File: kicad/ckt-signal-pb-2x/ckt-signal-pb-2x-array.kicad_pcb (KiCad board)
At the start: 2 copper layers, 81.9 x 157.4 mm, 144 parts, among them J1 Molex 0532610471, J2 Molex 0532610471

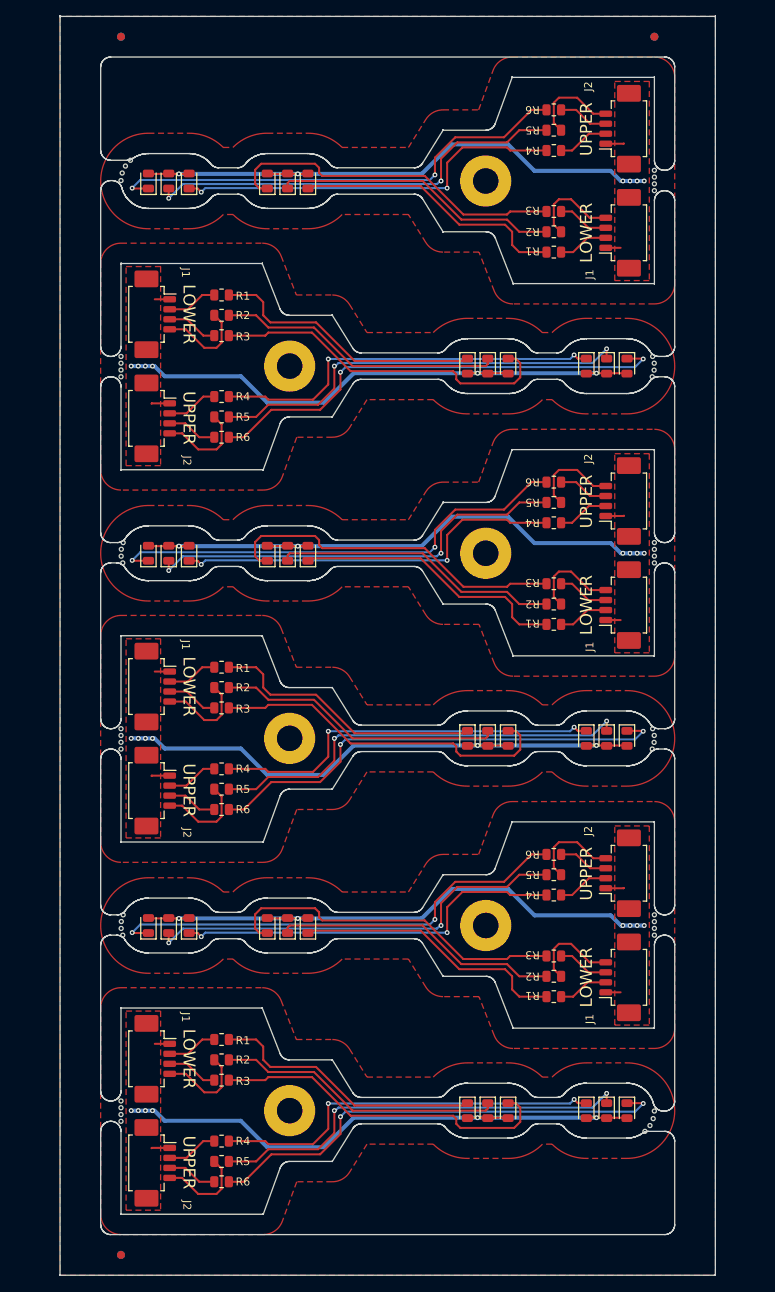
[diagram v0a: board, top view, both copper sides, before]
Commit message: Redesign 2x signal for better panelization
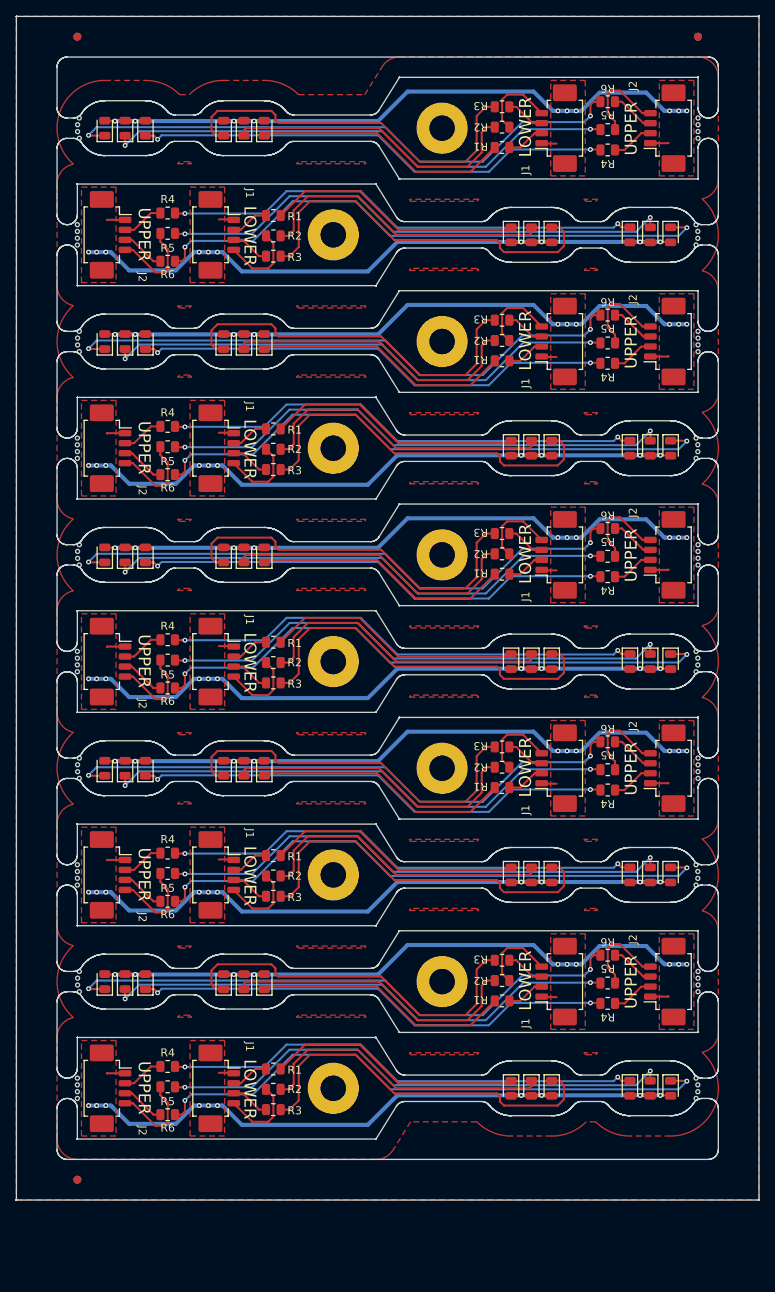
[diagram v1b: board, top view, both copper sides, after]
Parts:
- removed the D1 at (138.5, 133.6)
- removed the D1 at (138.5, 87.1)
- removed the D1 at (158.5, 156.8)
- removed the D1 at (158.5, 110.2)
- removed the D1 at (158.5, 63.7)
- removed the D1 at (138.5, 40.6)
- removed the D2 at (161.0, 156.8)
- removed the D2 at (136.0, 133.6)
- removed the D2 at (136.0, 87.1)
- removed the D2 at (161.0, 63.7)
- removed the D2 at (161.0, 110.2)
- removed the D2 at (136.0, 40.6)
- removed the D3 at (163.5, 63.7)
- removed the D3 at (133.5, 87.1)
- removed the D3 at (163.5, 110.2)
- removed the D3 at (133.5, 40.6)
- removed the D3 at (133.5, 133.6)
- removed the D3 at (163.5, 156.8)
- removed the D4 at (173.3, 156.8)
- removed the D4 at (173.3, 63.7)
- removed the D4 at (123.7, 40.6)
- removed the D4 at (123.7, 87.1)
- removed the D4 at (173.3, 110.2)
- removed the D4 at (123.7, 133.6)
- removed the D5 at (175.9, 110.2)
- removed the D5 at (121.1, 133.6)
- removed the D5 at (175.9, 156.8)
- removed the D5 at (121.1, 87.1)
- removed the D5 at (175.9, 63.7)
- removed the D5 at (121.1, 40.6)
- removed the D6 at (178.4, 156.8)
- removed the D6 at (118.6, 133.6)
- removed the D6 at (118.6, 87.1)
- removed the D6 at (178.4, 63.7)
- removed the D6 at (118.6, 40.6)
- removed the D6 at (178.4, 110.2)
- removed the H1 at (136.2, 156.8)
- removed the H1 at (136.2, 63.7)
- removed the H1 at (160.8, 40.6)
- removed the H1 at (160.8, 133.6)
- removed the H1 at (160.8, 87.1)
- removed the H1 at (136.2, 110.2)
- removed the J1 at (178.2, 93.6)
- removed the J1 at (178.2, 140.1)
- removed the J1 at (118.8, 150.3)
- removed the J1 at (118.8, 103.8)
- removed the J1 at (178.2, 47.1)
- removed the J1 at (118.8, 57.2)
- removed the J2 at (178.2, 127.1)
- removed the J2 at (118.8, 116.8)
- removed the J2 at (118.8, 163.3)
- removed the J2 at (118.8, 70.2)
- removed the J2 at (178.2, 80.6)
- removed the J2 at (178.2, 34.0)
- removed the R1 at (169.3, 49.5)
- removed the R1 at (169.3, 142.5)
- removed the R1 at (127.7, 147.9)
- removed the R1 at (127.7, 101.4)
- removed the R1 at (169.3, 96.0)
- removed the R1 at (127.7, 54.8)
- removed the R2 at (169.3, 93.5)
- removed the R2 at (127.7, 150.4)
- removed the R2 at (169.3, 140.0)
- removed the R2 at (127.7, 103.9)
- removed the R2 at (127.7, 57.4)
- removed the R2 at (169.3, 46.9)
- removed the R3 at (127.7, 59.9)
- removed the R3 at (169.3, 137.4)
- removed the R3 at (127.7, 153.0)
- removed the R3 at (169.3, 90.9)
- removed the R3 at (169.3, 44.4)
- removed the R3 at (127.7, 106.4)
- removed the R4 at (169.3, 129.8)
- removed the R4 at (127.7, 67.5)
- removed the R4 at (127.7, 114.1)
- removed the R4 at (127.7, 160.6)
- removed the R4 at (169.3, 83.3)
- removed the R4 at (169.3, 36.8)
- removed the R5 at (127.7, 116.6)
- removed the R5 at (169.3, 127.3)
- removed the R5 at (127.7, 70.1)
- removed the R5 at (169.3, 80.8)
- removed the R5 at (169.3, 34.2)
- removed the R5 at (127.7, 163.1)
- removed the R6 at (127.7, 165.7)
- removed the R6 at (169.3, 124.7)
- removed the R6 at (127.7, 72.6)
- removed the R6 at (169.3, 78.2)
- removed the R6 at (169.3, 31.7)
- removed the R6 at (127.7, 119.1)
- added D1: RED, LED_SMD:LED_0805_2012Metric, F.Cu at (133.1, 60.6)
- added D1: RED, LED_SMD:LED_0805_2012Metric, F.Cu at (163.9, 127.3)
- added D1: RED, LED_SMD:LED_0805_2012Metric, F.Cu at (133.1, 87.3)
- added D1: RED, LED_SMD:LED_0805_2012Metric, F.Cu at (133.1, 140.7)
- added D1: RED, LED_SMD:LED_0805_2012Metric, F.Cu at (163.9, 47.3)
- added D1: RED, LED_SMD:LED_0805_2012Metric, F.Cu at (133.1, 34.0)
- added D1: RED, LED_SMD:LED_0805_2012Metric, F.Cu at (133.1, 114.0)
- added D1: RED, LED_SMD:LED_0805_2012Metric, F.Cu at (163.9, 74.0)
- added D1: RED, LED_SMD:LED_0805_2012Metric, F.Cu at (163.9, 154.0)
- added D1: RED, LED_SMD:LED_0805_2012Metric, F.Cu at (163.9, 100.6)
- added D2: AMBER, LED_SMD:LED_0805_2012Metric, F.Cu at (130.5, 114.0)
- added D2: AMBER, LED_SMD:LED_0805_2012Metric, F.Cu at (166.5, 74.0)
- added D2: AMBER, LED_SMD:LED_0805_2012Metric, F.Cu at (130.5, 60.6)
- added D2: AMBER, LED_SMD:LED_0805_2012Metric, F.Cu at (130.5, 87.3)
- added D2: AMBER, LED_SMD:LED_0805_2012Metric, F.Cu at (130.5, 34.0)
- added D2: AMBER, LED_SMD:LED_0805_2012Metric, F.Cu at (130.5, 140.7)
- added D2: AMBER, LED_SMD:LED_0805_2012Metric, F.Cu at (166.5, 127.3)
- added D2: AMBER, LED_SMD:LED_0805_2012Metric, F.Cu at (166.5, 47.3)
- added D2: AMBER, LED_SMD:LED_0805_2012Metric, F.Cu at (166.5, 154.0)
- added D2: AMBER, LED_SMD:LED_0805_2012Metric, F.Cu at (166.5, 100.6)
- added D3: GREEN, LED_SMD:LED_0805_2012Metric, F.Cu at (128.0, 87.3)
- added D3: GREEN, LED_SMD:LED_0805_2012Metric, F.Cu at (169.0, 100.6)
- added D3: GREEN, LED_SMD:LED_0805_2012Metric, F.Cu at (169.0, 74.0)
- added D3: GREEN, LED_SMD:LED_0805_2012Metric, F.Cu at (128.0, 114.0)
- added D3: GREEN, LED_SMD:LED_0805_2012Metric, F.Cu at (128.0, 34.0)
- added D3: GREEN, LED_SMD:LED_0805_2012Metric, F.Cu at (128.0, 60.6)
- added D3: GREEN, LED_SMD:LED_0805_2012Metric, F.Cu at (128.0, 140.7)
- added D3: GREEN, LED_SMD:LED_0805_2012Metric, F.Cu at (169.0, 47.3)
- added D3: GREEN, LED_SMD:LED_0805_2012Metric, F.Cu at (169.0, 127.3)
- added D3: GREEN, LED_SMD:LED_0805_2012Metric, F.Cu at (169.0, 154.0)
- added D4: RED, LED_SMD:LED_0805_2012Metric, F.Cu at (118.2, 87.3)
- added D4: RED, LED_SMD:LED_0805_2012Metric, F.Cu at (118.2, 140.7)
- added D4: RED, LED_SMD:LED_0805_2012Metric, F.Cu at (178.8, 47.3)
- added D4: RED, LED_SMD:LED_0805_2012Metric, F.Cu at (178.8, 127.3)
- added D4: RED, LED_SMD:LED_0805_2012Metric, F.Cu at (178.8, 154.0)
- added D4: RED, LED_SMD:LED_0805_2012Metric, F.Cu at (118.2, 60.6)
- added D4: RED, LED_SMD:LED_0805_2012Metric, F.Cu at (178.8, 100.6)
- added D4: RED, LED_SMD:LED_0805_2012Metric, F.Cu at (118.2, 34.0)
- added D4: RED, LED_SMD:LED_0805_2012Metric, F.Cu at (178.8, 74.0)
- added D4: RED, LED_SMD:LED_0805_2012Metric, F.Cu at (118.2, 114.0)
- added D5: AMBER, LED_SMD:LED_0805_2012Metric, F.Cu at (181.3, 100.6)
- added D5: AMBER, LED_SMD:LED_0805_2012Metric, F.Cu at (115.7, 114.0)
- added D5: AMBER, LED_SMD:LED_0805_2012Metric, F.Cu at (181.3, 74.0)
- added D5: AMBER, LED_SMD:LED_0805_2012Metric, F.Cu at (115.7, 34.0)
- added D5: AMBER, LED_SMD:LED_0805_2012Metric, F.Cu at (181.3, 127.3)
- added D5: AMBER, LED_SMD:LED_0805_2012Metric, F.Cu at (115.7, 87.3)
- added D5: AMBER, LED_SMD:LED_0805_2012Metric, F.Cu at (115.7, 140.7)
- added D5: AMBER, LED_SMD:LED_0805_2012Metric, F.Cu at (181.3, 47.3)
- added D5: AMBER, LED_SMD:LED_0805_2012Metric, F.Cu at (115.7, 60.6)
- added D5: AMBER, LED_SMD:LED_0805_2012Metric, F.Cu at (181.3, 154.0)
- added D6: GREEN, LED_SMD:LED_0805_2012Metric, F.Cu at (183.9, 154.0)
- added D6: GREEN, LED_SMD:LED_0805_2012Metric, F.Cu at (183.9, 127.3)
- added D6: GREEN, LED_SMD:LED_0805_2012Metric, F.Cu at (183.9, 74.0)
- added D6: GREEN, LED_SMD:LED_0805_2012Metric, F.Cu at (113.1, 87.3)
- added D6: GREEN, LED_SMD:LED_0805_2012Metric, F.Cu at (113.1, 60.6)
- added D6: GREEN, LED_SMD:LED_0805_2012Metric, F.Cu at (113.1, 34.0)
- added D6: GREEN, LED_SMD:LED_0805_2012Metric, F.Cu at (113.1, 114.0)
- added D6: GREEN, LED_SMD:LED_0805_2012Metric, F.Cu at (183.9, 47.3)
- added D6: GREEN, LED_SMD:LED_0805_2012Metric, F.Cu at (183.9, 100.6)
- added D6: GREEN, LED_SMD:LED_0805_2012Metric, F.Cu at (113.1, 140.7)
- added H1: MountingHole, MountingHole:MountingHole_3.2mm_M3_Pad, F.Cu at (155.3, 34.0)
- added H1: MountingHole, MountingHole:MountingHole_3.2mm_M3_Pad, F.Cu at (141.7, 100.6)
- added H1: MountingHole, MountingHole:MountingHole_3.2mm_M3_Pad, F.Cu at (155.3, 60.6)
- added H1: MountingHole, MountingHole:MountingHole_3.2mm_M3_Pad, F.Cu at (141.7, 74.0)
- added H1: MountingHole, MountingHole:MountingHole_3.2mm_M3_Pad, F.Cu at (155.3, 140.7)
- added H1: MountingHole, MountingHole:MountingHole_3.2mm_M3_Pad, F.Cu at (155.3, 114.0)
- added H1: MountingHole, MountingHole:MountingHole_3.2mm_M3_Pad, F.Cu at (141.7, 154.0)
- added H1: MountingHole, MountingHole:MountingHole_3.2mm_M3_Pad, F.Cu at (141.7, 127.3)
- added H1: MountingHole, MountingHole:MountingHole_3.2mm_M3_Pad, F.Cu at (141.7, 47.3)
- added H1: MountingHole, MountingHole:MountingHole_3.2mm_M3_Pad, F.Cu at (155.3, 87.3)
- added J1: Molex 0532610471, Connector_Molex:Molex_PicoBlade_53261-0471_1x04-1MP_P1.25mm_Horizontal, F.Cu at (170.1, 140.7)
- added J1: Molex 0532610471, Connector_Molex:Molex_PicoBlade_53261-0471_1x04-1MP_P1.25mm_Horizontal, F.Cu at (126.9, 154.0)
- added J1: Molex 0532610471, Connector_Molex:Molex_PicoBlade_53261-0471_1x04-1MP_P1.25mm_Horizontal, F.Cu at (170.1, 34.0)
- added J1: Molex 0532610471, Connector_Molex:Molex_PicoBlade_53261-0471_1x04-1MP_P1.25mm_Horizontal, F.Cu at (170.1, 114.0)
- added J1: Molex 0532610471, Connector_Molex:Molex_PicoBlade_53261-0471_1x04-1MP_P1.25mm_Horizontal, F.Cu at (126.9, 100.6)
- added J1: Molex 0532610471, Connector_Molex:Molex_PicoBlade_53261-0471_1x04-1MP_P1.25mm_Horizontal, F.Cu at (126.9, 74.0)
- added J1: Molex 0532610471, Connector_Molex:Molex_PicoBlade_53261-0471_1x04-1MP_P1.25mm_Horizontal, F.Cu at (126.9, 127.3)
- added J1: Molex 0532610471, Connector_Molex:Molex_PicoBlade_53261-0471_1x04-1MP_P1.25mm_Horizontal, F.Cu at (126.9, 47.3)
- added J1: Molex 0532610471, Connector_Molex:Molex_PicoBlade_53261-0471_1x04-1MP_P1.25mm_Horizontal, F.Cu at (170.1, 60.6)
- added J1: Molex 0532610471, Connector_Molex:Molex_PicoBlade_53261-0471_1x04-1MP_P1.25mm_Horizontal, F.Cu at (170.1, 87.3)
- added J2: Molex 0532610471, Connector_Molex:Molex_PicoBlade_53261-0471_1x04-1MP_P1.25mm_Horizontal, F.Cu at (113.3, 127.3)
- added J2: Molex 0532610471, Connector_Molex:Molex_PicoBlade_53261-0471_1x04-1MP_P1.25mm_Horizontal, F.Cu at (113.3, 74.0)
- added J2: Molex 0532610471, Connector_Molex:Molex_PicoBlade_53261-0471_1x04-1MP_P1.25mm_Horizontal, F.Cu at (113.3, 100.6)
- added J2: Molex 0532610471, Connector_Molex:Molex_PicoBlade_53261-0471_1x04-1MP_P1.25mm_Horizontal, F.Cu at (183.7, 60.6)
- added J2: Molex 0532610471, Connector_Molex:Molex_PicoBlade_53261-0471_1x04-1MP_P1.25mm_Horizontal, F.Cu at (183.7, 34.0)
- added J2: Molex 0532610471, Connector_Molex:Molex_PicoBlade_53261-0471_1x04-1MP_P1.25mm_Horizontal, F.Cu at (183.7, 140.7)
- added J2: Molex 0532610471, Connector_Molex:Molex_PicoBlade_53261-0471_1x04-1MP_P1.25mm_Horizontal, F.Cu at (183.7, 114.0)
- added J2: Molex 0532610471, Connector_Molex:Molex_PicoBlade_53261-0471_1x04-1MP_P1.25mm_Horizontal, F.Cu at (113.3, 154.0)
- added J2: Molex 0532610471, Connector_Molex:Molex_PicoBlade_53261-0471_1x04-1MP_P1.25mm_Horizontal, F.Cu at (113.3, 47.3)
- added J2: Molex 0532610471, Connector_Molex:Molex_PicoBlade_53261-0471_1x04-1MP_P1.25mm_Horizontal, F.Cu at (183.7, 87.3)
- added KiKit_MB_13_1: NPTH, NPTH, F.Cu at (110.0, 115.2)
- added KiKit_MB_13_2: NPTH, NPTH, F.Cu at (109.7, 114.4)
- added KiKit_MB_13_3: NPTH, NPTH, F.Cu at (109.7, 113.5)
- added KiKit_MB_13_4: NPTH, NPTH, F.Cu at (110.0, 112.7)
- added KiKit_MB_14_1: NPTH, NPTH, F.Cu at (187.3, 112.7)
- added KiKit_MB_14_2: NPTH, NPTH, F.Cu at (187.3, 113.6)
- added KiKit_MB_14_3: NPTH, NPTH, F.Cu at (187.3, 114.4)
- added KiKit_MB_14_4: NPTH, NPTH, F.Cu at (187.3, 115.2)
- added KiKit_MB_15_1: NPTH, NPTH, F.Cu at (109.7, 128.6)
- added KiKit_MB_15_2: NPTH, NPTH, F.Cu at (109.7, 127.7)
- added KiKit_MB_15_3: NPTH, NPTH, F.Cu at (109.7, 126.9)
- added KiKit_MB_15_4: NPTH, NPTH, F.Cu at (109.7, 126.0)
- added KiKit_MB_16_1: NPTH, NPTH, F.Cu at (187.0, 126.0)
- added KiKit_MB_16_2: NPTH, NPTH, F.Cu at (187.3, 126.9)
- added KiKit_MB_16_3: NPTH, NPTH, F.Cu at (187.3, 127.7)
- added KiKit_MB_16_4: NPTH, NPTH, F.Cu at (187.0, 128.6)
- added KiKit_MB_17_1: NPTH, NPTH, F.Cu at (110.0, 141.9)
- added KiKit_MB_17_2: NPTH, NPTH, F.Cu at (109.7, 141.1)
- added KiKit_MB_17_3: NPTH, NPTH, F.Cu at (109.7, 140.2)
- added KiKit_MB_17_4: NPTH, NPTH, F.Cu at (110.0, 139.4)
- added KiKit_MB_18_1: NPTH, NPTH, F.Cu at (187.3, 139.4)
- added KiKit_MB_18_2: NPTH, NPTH, F.Cu at (187.3, 140.2)
- added KiKit_MB_18_3: NPTH, NPTH, F.Cu at (187.3, 141.1)
- added KiKit_MB_18_4: NPTH, NPTH, F.Cu at (187.3, 141.9)
- added KiKit_MB_19_1: NPTH, NPTH, F.Cu at (109.7, 155.3)
- added KiKit_MB_19_2: NPTH, NPTH, F.Cu at (109.7, 154.4)
- added KiKit_MB_19_3: NPTH, NPTH, F.Cu at (109.7, 153.6)
- added KiKit_MB_19_4: NPTH, NPTH, F.Cu at (109.7, 152.7)
- added KiKit_MB_20_1: NPTH, NPTH, F.Cu at (187.0, 152.7)
- added KiKit_MB_20_2: NPTH, NPTH, F.Cu at (187.3, 153.6)
- added KiKit_MB_20_3: NPTH, NPTH, F.Cu at (187.3, 154.4)
- added KiKit_MB_20_4: NPTH, NPTH, F.Cu at (187.0, 155.3)
- added R1: 1k, Resistor_SMD:R_0805_2012Metric, F.Cu at (162.8, 36.4)
- added R1: 1k, Resistor_SMD:R_0805_2012Metric, F.Cu at (162.8, 116.4)
- added R1: 1k, Resistor_SMD:R_0805_2012Metric, F.Cu at (162.8, 89.7)
- added R1: 1k, Resistor_SMD:R_0805_2012Metric, F.Cu at (134.2, 44.9)
- added R1: 1k, Resistor_SMD:R_0805_2012Metric, F.Cu at (134.2, 71.6)
- added R1: 1k, Resistor_SMD:R_0805_2012Metric, F.Cu at (162.8, 63.1)
- added R1: 1k, Resistor_SMD:R_0805_2012Metric, F.Cu at (134.2, 98.2)
- added R1: 1k, Resistor_SMD:R_0805_2012Metric, F.Cu at (134.2, 151.6)
- added R1: 1k, Resistor_SMD:R_0805_2012Metric, F.Cu at (162.8, 143.1)
- added R1: 1k, Resistor_SMD:R_0805_2012Metric, F.Cu at (134.2, 124.9)
- added R2: 1k, Resistor_SMD:R_0805_2012Metric, F.Cu at (134.2, 100.8)
- added R2: 1k, Resistor_SMD:R_0805_2012Metric, F.Cu at (162.8, 60.5)
- added R2: 1k, Resistor_SMD:R_0805_2012Metric, F.Cu at (162.8, 33.8)
- added R2: 1k, Resistor_SMD:R_0805_2012Metric, F.Cu at (134.2, 127.4)
- added R2: 1k, Resistor_SMD:R_0805_2012Metric, F.Cu at (162.8, 113.9)
- added R2: 1k, Resistor_SMD:R_0805_2012Metric, F.Cu at (134.2, 74.1)
- added R2: 1k, Resistor_SMD:R_0805_2012Metric, F.Cu at (162.8, 87.2)
- added R2: 1k, Resistor_SMD:R_0805_2012Metric, F.Cu at (162.8, 140.5)
- added R2: 1k, Resistor_SMD:R_0805_2012Metric, F.Cu at (134.2, 47.4)
- added R2: 1k, Resistor_SMD:R_0805_2012Metric, F.Cu at (134.2, 154.1)
- added R3: 1k, Resistor_SMD:R_0805_2012Metric, F.Cu at (162.8, 138.0)
- added R3: 1k, Resistor_SMD:R_0805_2012Metric, F.Cu at (162.8, 58.0)
- added R3: 1k, Resistor_SMD:R_0805_2012Metric, F.Cu at (134.2, 156.7)
- added R3: 1k, Resistor_SMD:R_0805_2012Metric, F.Cu at (162.8, 111.3)
- added R3: 1k, Resistor_SMD:R_0805_2012Metric, F.Cu at (134.2, 103.3)
- added R3: 1k, Resistor_SMD:R_0805_2012Metric, F.Cu at (134.2, 76.6)
- added R3: 1k, Resistor_SMD:R_0805_2012Metric, F.Cu at (134.2, 130.0)
- added R3: 1k, Resistor_SMD:R_0805_2012Metric, F.Cu at (134.2, 50.0)
- added R3: 1k, Resistor_SMD:R_0805_2012Metric, F.Cu at (162.8, 84.6)
- added R3: 1k, Resistor_SMD:R_0805_2012Metric, F.Cu at (162.8, 31.3)
- added R4: 1k, Resistor_SMD:R_0805_2012Metric, F.Cu at (176.0, 90.0)
- added R4: 1k, Resistor_SMD:R_0805_2012Metric, F.Cu at (176.0, 36.7)
- added R4: 1k, Resistor_SMD:R_0805_2012Metric, F.Cu at (121.0, 151.3)
- added R4: 1k, Resistor_SMD:R_0805_2012Metric, F.Cu at (121.0, 44.6)
- added R4: 1k, Resistor_SMD:R_0805_2012Metric, F.Cu at (121.0, 71.3)
- added R4: 1k, Resistor_SMD:R_0805_2012Metric, F.Cu at (176.0, 63.4)
- added R4: 1k, Resistor_SMD:R_0805_2012Metric, F.Cu at (121.0, 97.9)
- added R4: 1k, Resistor_SMD:R_0805_2012Metric, F.Cu at (121.0, 124.6)
- added R4: 1k, Resistor_SMD:R_0805_2012Metric, F.Cu at (176.0, 143.4)
- added R4: 1k, Resistor_SMD:R_0805_2012Metric, F.Cu at (176.0, 116.7)
- added R5: 1k, Resistor_SMD:R_0805_2012Metric, F.Cu at (121.0, 153.8)
- added R5: 1k, Resistor_SMD:R_0805_2012Metric, F.Cu at (176.0, 60.8)
- added R5: 1k, Resistor_SMD:R_0805_2012Metric, F.Cu at (176.0, 34.2)
- added R5: 1k, Resistor_SMD:R_0805_2012Metric, F.Cu at (121.0, 100.5)
- added R5: 1k, Resistor_SMD:R_0805_2012Metric, F.Cu at (121.0, 127.1)
- added R5: 1k, Resistor_SMD:R_0805_2012Metric, F.Cu at (121.0, 47.1)
- added R5: 1k, Resistor_SMD:R_0805_2012Metric, F.Cu at (121.0, 73.8)
- added R5: 1k, Resistor_SMD:R_0805_2012Metric, F.Cu at (176.0, 114.2)
- added R5: 1k, Resistor_SMD:R_0805_2012Metric, F.Cu at (176.0, 87.5)
- added R5: 1k, Resistor_SMD:R_0805_2012Metric, F.Cu at (176.0, 140.8)
- added R6: 1k, Resistor_SMD:R_0805_2012Metric, F.Cu at (121.0, 50.6)
- added R6: 1k, Resistor_SMD:R_0805_2012Metric, F.Cu at (176.0, 57.3)
- added R6: 1k, Resistor_SMD:R_0805_2012Metric, F.Cu at (121.0, 103.9)
- added R6: 1k, Resistor_SMD:R_0805_2012Metric, F.Cu at (176.0, 84.0)
- added R6: 1k, Resistor_SMD:R_0805_2012Metric, F.Cu at (121.0, 130.6)
- added R6: 1k, Resistor_SMD:R_0805_2012Metric, F.Cu at (176.0, 110.7)
- added R6: 1k, Resistor_SMD:R_0805_2012Metric, F.Cu at (176.0, 137.3)
- added R6: 1k, Resistor_SMD:R_0805_2012Metric, F.Cu at (121.0, 157.3)
- added R6: 1k, Resistor_SMD:R_0805_2012Metric, F.Cu at (176.0, 30.7)
- added R6: 1k, Resistor_SMD:R_0805_2012Metric, F.Cu at (121.0, 77.3)
- moved KiKit_MB_12_3 57.9 mm to (187.3, 101.1)
- moved KiKit_MB_12_2 57.8 mm to (187.3, 100.2)
- moved KiKit_MB_12_4 57.8 mm to (187.0, 101.9)
- moved KiKit_MB_12_1 57.7 mm to (187.0, 99.4)
- moved KiKit_MB_11_1 56.5 mm to (109.7, 101.9)
- moved KiKit_MB_11_2 56.5 mm to (109.7, 101.1)
- moved KiKit_MB_11_3 56.5 mm to (109.7, 100.2)
- moved KiKit_MB_11_4 56.5 mm to (109.7, 99.4)
- moved KiKit_MB_9_4 46.6 mm to (110.0, 86.0)
- moved KiKit_MB_10_2 46.6 mm to (187.3, 86.9)
- moved KiKit_MB_10_3 46.6 mm to (187.3, 87.7)
- moved KiKit_MB_10_4 46.6 mm to (187.3, 88.6)
- moved KiKit_MB_10_1 46.6 mm to (187.3, 86.0)
- moved KiKit_MB_9_1 46.6 mm to (110.0, 88.6)
- moved KiKit_MB_9_3 46.6 mm to (109.7, 86.9)
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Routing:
- net Board_9-Net-(D1-Pad2): track 0.00 -> 90.3 mm, vias 0 -> 10
- net Board_8-Net-(D1-Pad2): track 0.00 -> 90.3 mm, vias 0 -> 10
- net Board_7-Net-(D1-Pad2): track 0.00 -> 90.3 mm, vias 0 -> 10
- net Board_6-Net-(D1-Pad2): track 0.00 -> 90.3 mm, vias 0 -> 10
- net Board_6-Net-(D6-Pad1): track 0.00 -> 72.2 mm, vias 0 -> 2
- net Board_7-Net-(D6-Pad1): track 0.00 -> 72.2 mm, vias 0 -> 2
- net Board_8-Net-(D6-Pad1): track 0.00 -> 72.2 mm, vias 0 -> 2
- net Board_9-Net-(D6-Pad1): track 0.00 -> 72.2 mm, vias 0 -> 2
- net Board_9-Net-(D5-Pad1): track 0.00 -> 65.2 mm, vias 0 -> 2
- net Board_8-Net-(D5-Pad1): track 0.00 -> 65.2 mm, vias 0 -> 2
- net Board_7-Net-(D5-Pad1): track 0.00 -> 65.2 mm, vias 0 -> 2
- net Board_6-Net-(D5-Pad1): track 0.00 -> 65.2 mm, vias 0 -> 2
- net Board_9-Net-(D4-Pad1): track 0.00 -> 60.3 mm, vias 0 -> 2
- net Board_6-Net-(D4-Pad1): track 0.00 -> 60.3 mm, vias 0 -> 2
- net Board_7-Net-(D4-Pad1): track 0.00 -> 60.3 mm, vias 0 -> 2
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- added copper zone on F.Cu, net Board_6-Net-(D1-Pad2)
- added copper zone on F.Cu, net Board_7-Net-(D1-Pad2)
- added copper zone on F.Cu, net Board_8-Net-(D1-Pad2)
- added copper zone on F.Cu, net Board_9-Net-(D1-Pad2)
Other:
- board size 81.9 x 157.4 mm -> 92.8 x 148 mm
- board text added: "Iowa Scaled Engineering CKT-SIGNAL-PB-2X v3.0 ©2025 www.iascaled.com"
- board text removed: "Iowa Scaled Engineering CKT-SIGNAL-2X-PB v3.0 ©2025 www.iascaled.com"
